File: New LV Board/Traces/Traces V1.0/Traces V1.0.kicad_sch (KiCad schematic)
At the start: 13 parts, among them J1 B15B-PH-K-S, J2 B15B-PH-K-S, J3 B15B-PH-K-S, J4 Conn_01x12, J5 VBATT +, J6 Conn_01x12, J7 Conn_01x12, J8 Vs

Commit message: minor changes to traces
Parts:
- removed D1: BZV55B15, Diode_SMD:D_SC-80_HandSoldering, symbol BZV55B15:BZV55B15
- removed TP1, TP2: 5006, TestPoint:TestPoint_Keystone_5010-5014_Multipurpose, symbol 5006:5006
- added D2: D_Zener, Diode_SMD:D_1210_3225Metric, symbol Device:D_Zener
- added TP3, TP4: TestPoint, TestPoint:TestPoint_Keystone_5005-5009_Compact, symbol Connector:TestPoint
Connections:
- net at C2.1, J5.1, J8.2: now also D2.2 (A), TP4.1
- net at C2.2, F1.1, F1.2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: now also D2.1 (K), TP3.1
- net at J1.2, J4.10 (Pin_10), J4.11 (Pin_11)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: now also J7.8 (Pin_8); no longer J7.1 (Pin_1), J7.2 (Pin_2), J7.7 (Pin_7)
- net at J1.3, J4.7 (Pin_7), J6.8 (Pin_8): now also J7.4 (Pin_4); no longer J7.8 (Pin_8)
- net at J1.7: now also J7.2 (Pin_2); no longer J7.6 (Pin_6)
- net at J3.4: now also J7.1 (Pin_1); no longer J7.12 (Pin_12)
- net at J4.6 (Pin_6), J4.8 (Pin_8), J6.7 (Pin_7): now also J7.7 (Pin_7); no longer J7.3 (Pin_3), J7.9 (Pin_9)
- net at J7.5 (Pin_5): now also J3.6; no longer J3.1
- net at J3.7: now also J7.6 (Pin_6)
- new net: J3.5, J7.3 (Pin_3)
- now unconnected: J7.10 (Pin_10)
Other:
- note added: "5v"
- note added: "From PC"
- note added: "From enable switch"
- note added: "PC Status"
- note added: "VCU - Throttle latchinG"
- note added: "VCU Charge Enable"
- note removed: "5V+"
- note removed: "PC STATUS"
- note removed: "Precharge COIL"
- note removed: "TSMS VS"
- note removed: "VCU - Throttle latching - Precharge"

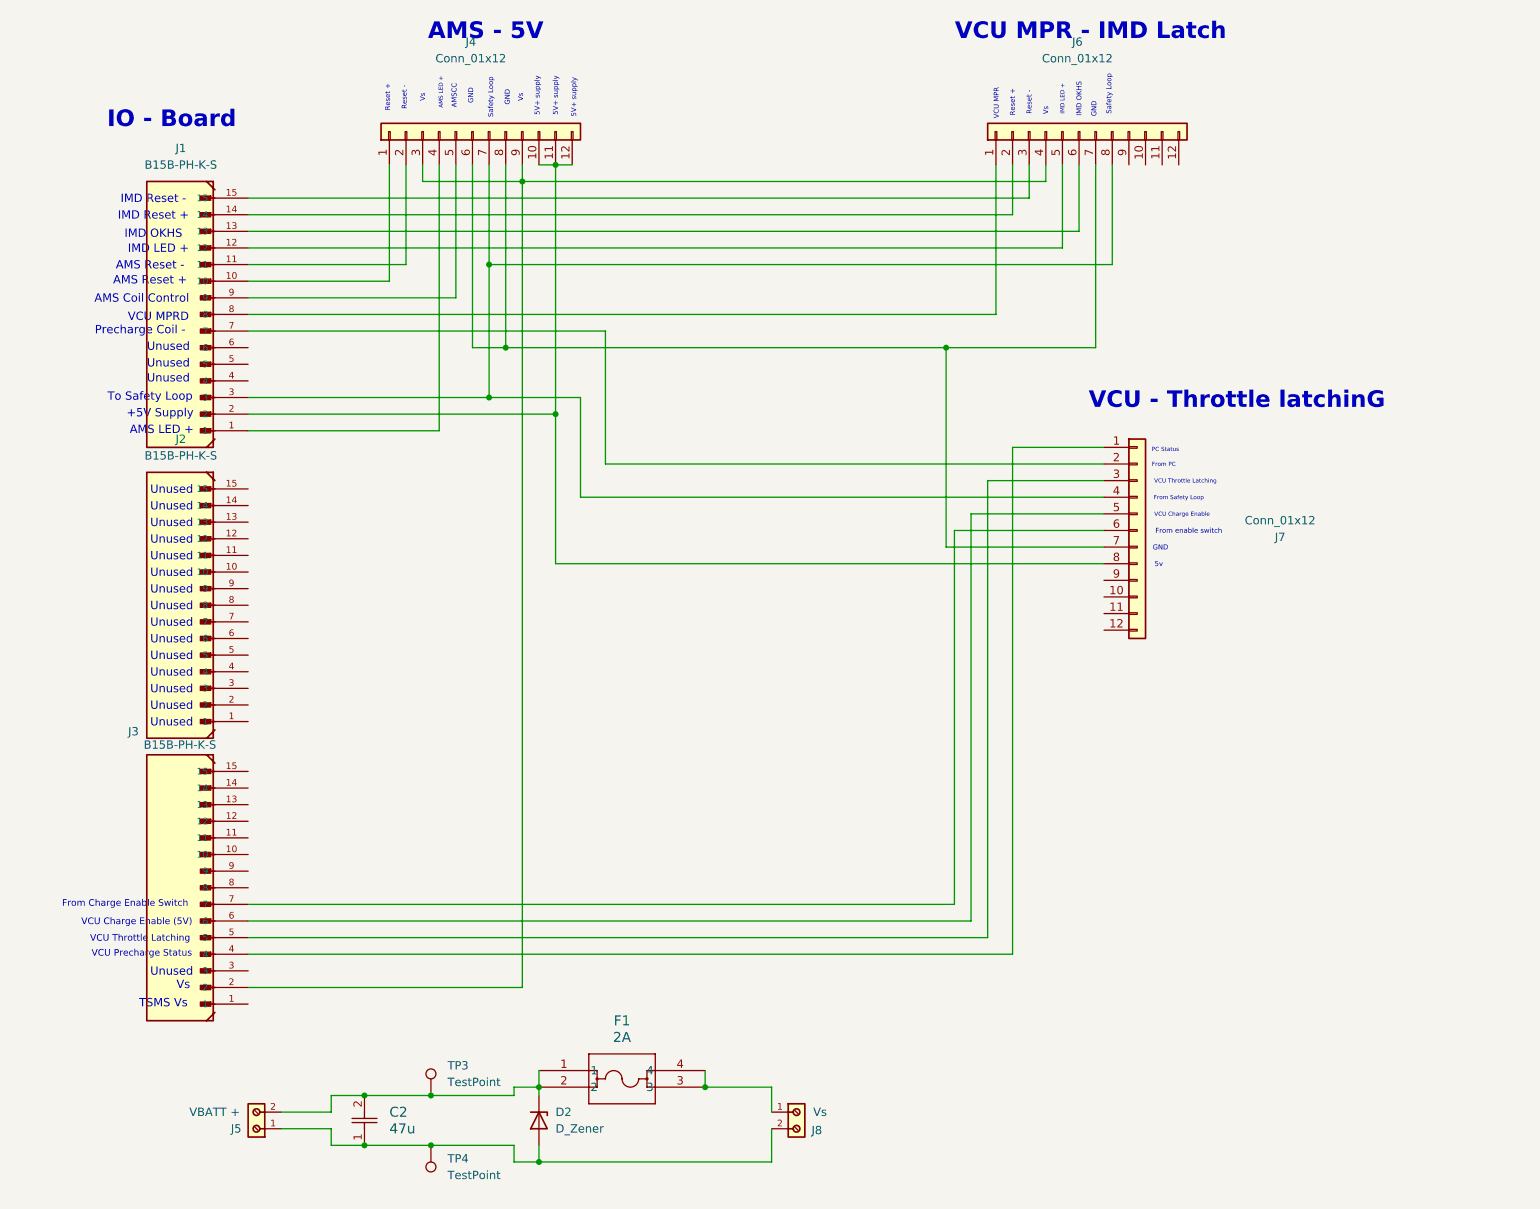
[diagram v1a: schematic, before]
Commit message: minor power changes to traces schematic
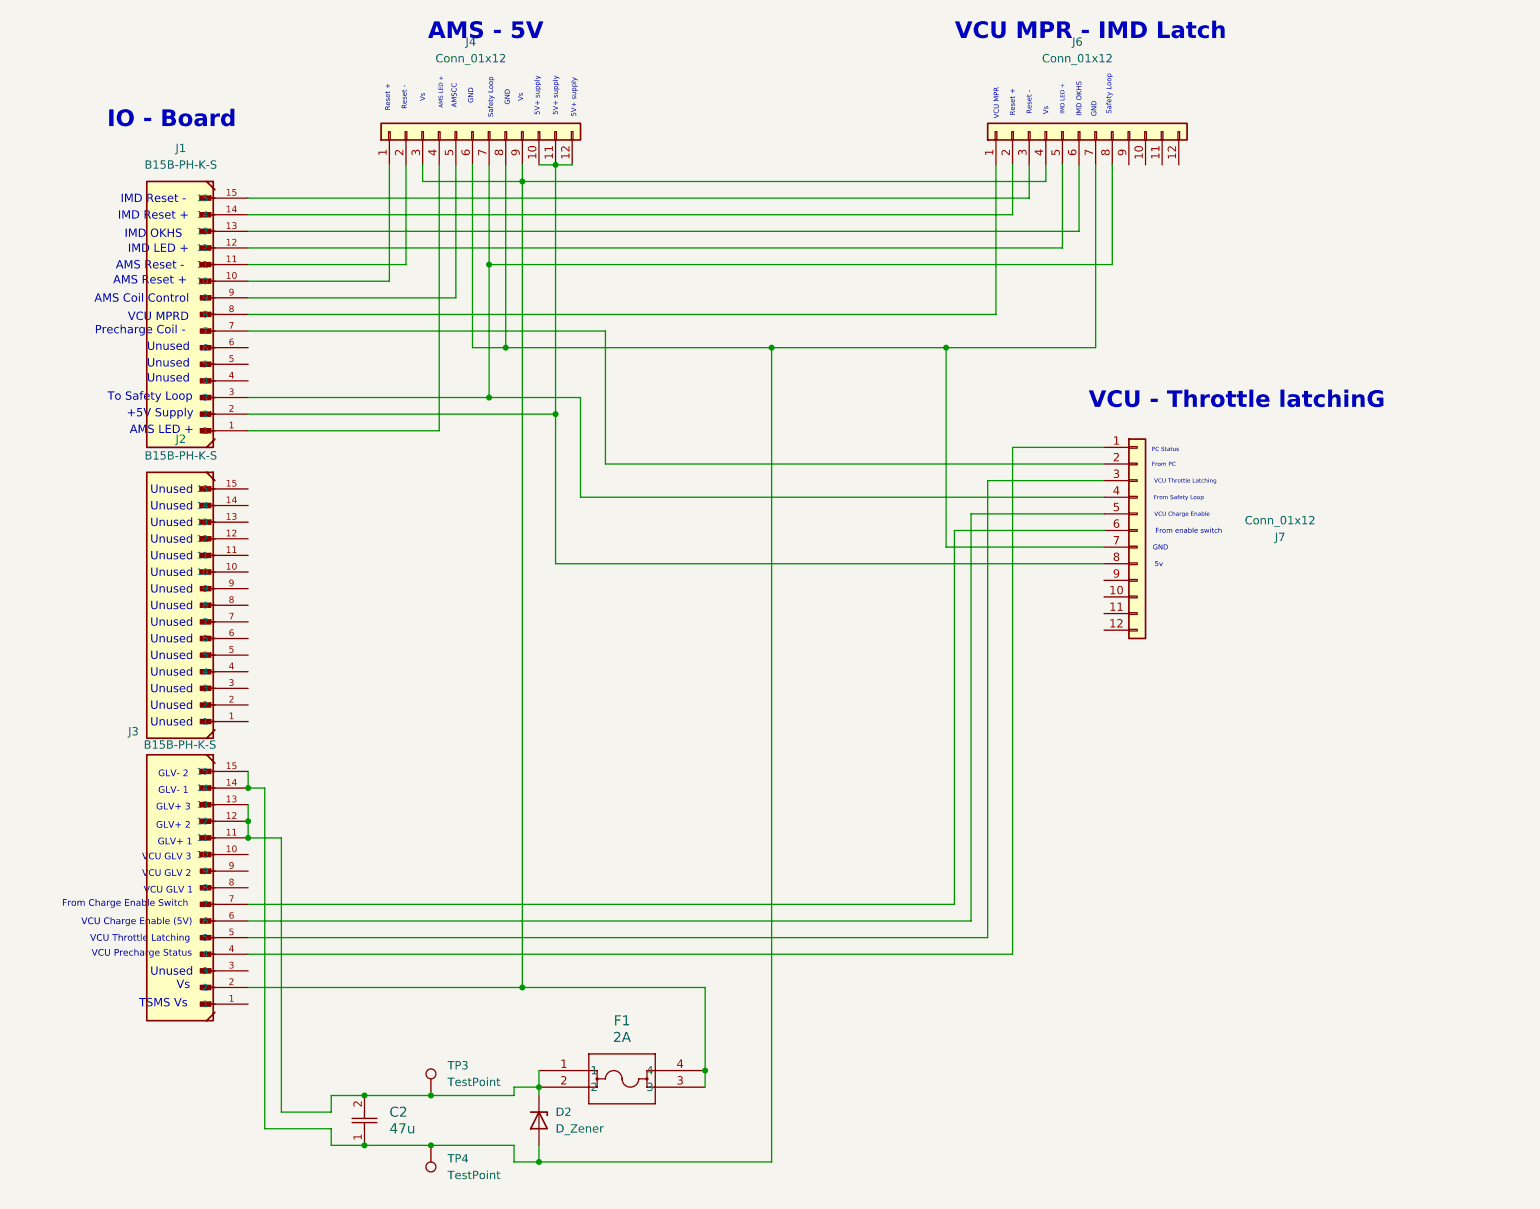
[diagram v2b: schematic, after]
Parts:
- removed J5: VBATT +, motorsports:691137710002, symbol 691137710002:691137710002
- removed J8: Vs, motorsports:691137710002, symbol 691137710002:691137710002
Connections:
- net at C2.1, D2.2 (A), TP4.1: now also J3.14, J3.15, J4.6 (Pin_6), J4.8 (Pin_8), J6.7 (Pin_7), J7.7 (Pin_7)
- net at C2.2, D2.1 (K), F1.1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: now also J3.11, J3.12, J3.13
- net at F1.3, F1.4: now also J3.2, J4.3 (Pin_3), J4.9 (Pin_9), J6.4 (Pin_4)
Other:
- note added: "GLV+ 1"
- note added: "GLV+ 2"
- note added: "GLV+ 3"
- note added: "GLV- 1"
- note added: "GLV- 2"
- note added: "VCU GLV 1"
- note added: "VCU GLV 2"
- note added: "VCU GLV 3"

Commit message: vcu throttle latching connected to traces
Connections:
- net at F1.3, F1.4, J4.3 (Pin_3)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: now also J3.4; no longer J3.2
- net at J7.1 (Pin_1): now also J3.5; no longer J3.4
- net at J7.3 (Pin_3): now also J3.6; no longer J3.5
- net at J7.5 (Pin_5): now also J3.7; no longer J3.6
- net at J7.6 (Pin_6): now also J3.8; no longer J3.7
- net at J3.1: now also J3.10, J3.9
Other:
- note added: "VCU - Throttle latching"
- note removed: "TSMS Vs"
- note removed: "VCU - Throttle latchinG"

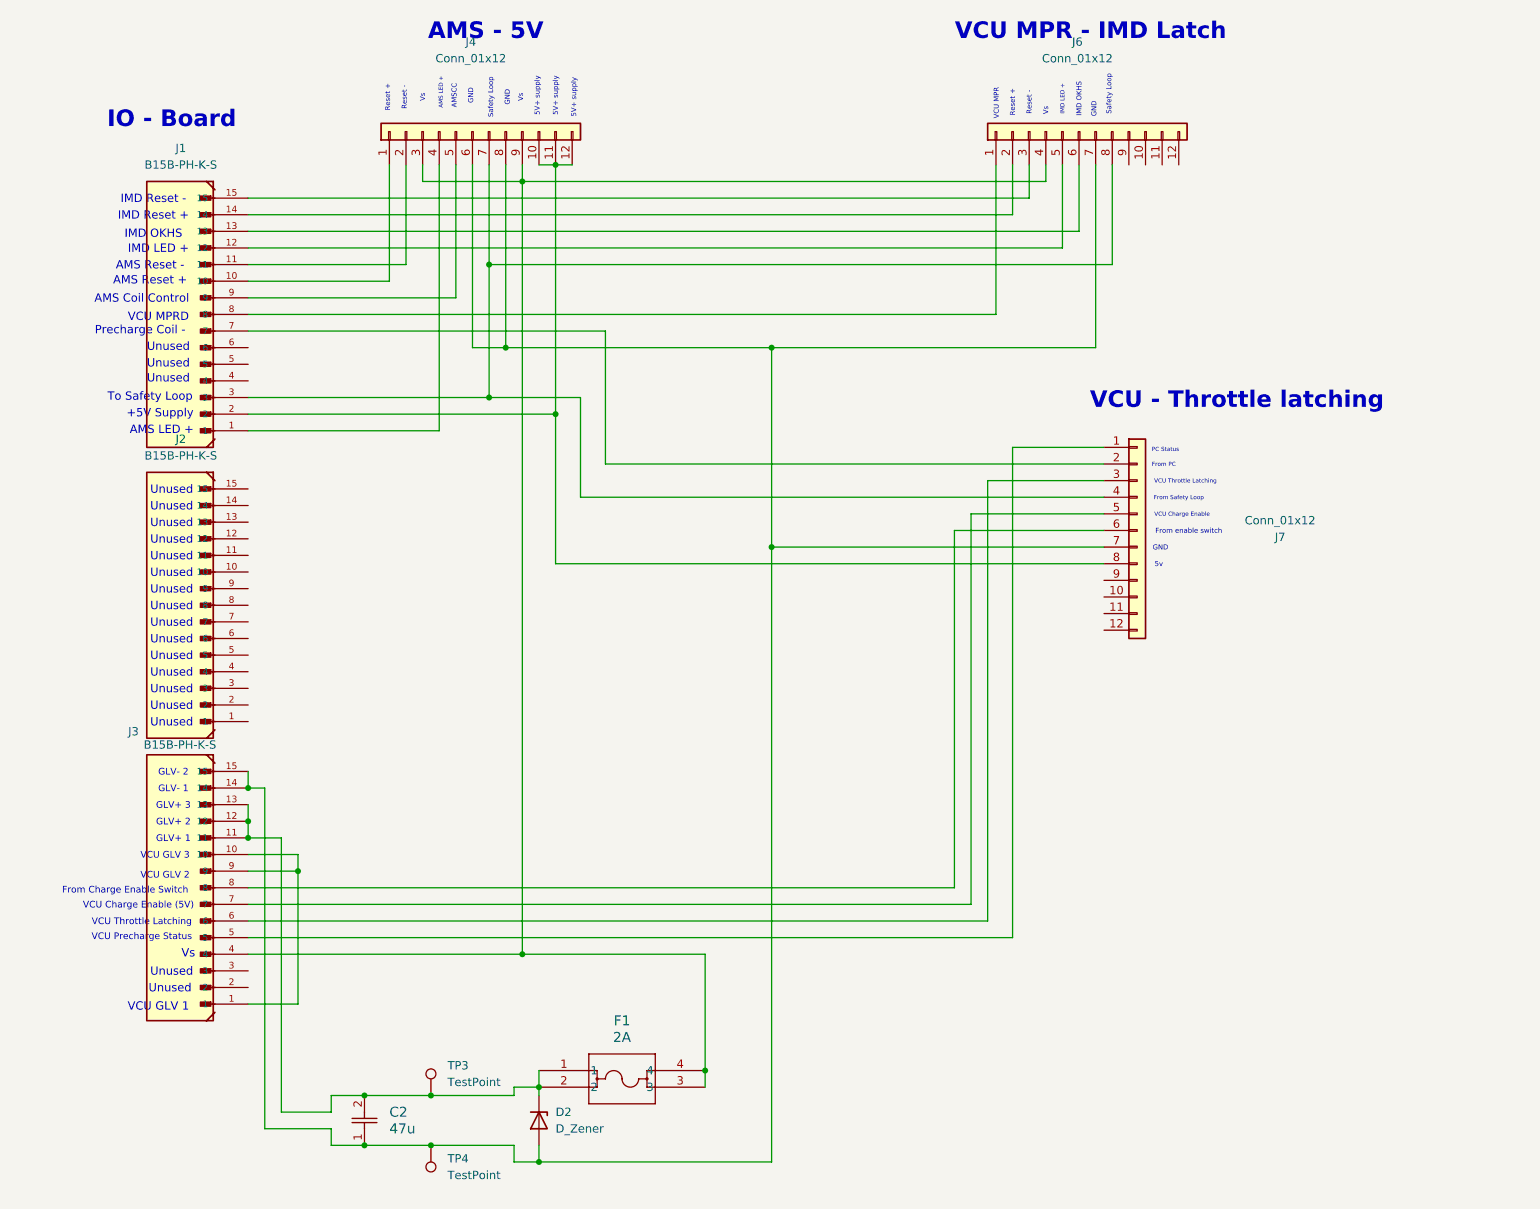
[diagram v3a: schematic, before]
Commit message: added VCU MPR - 5V to scehematic
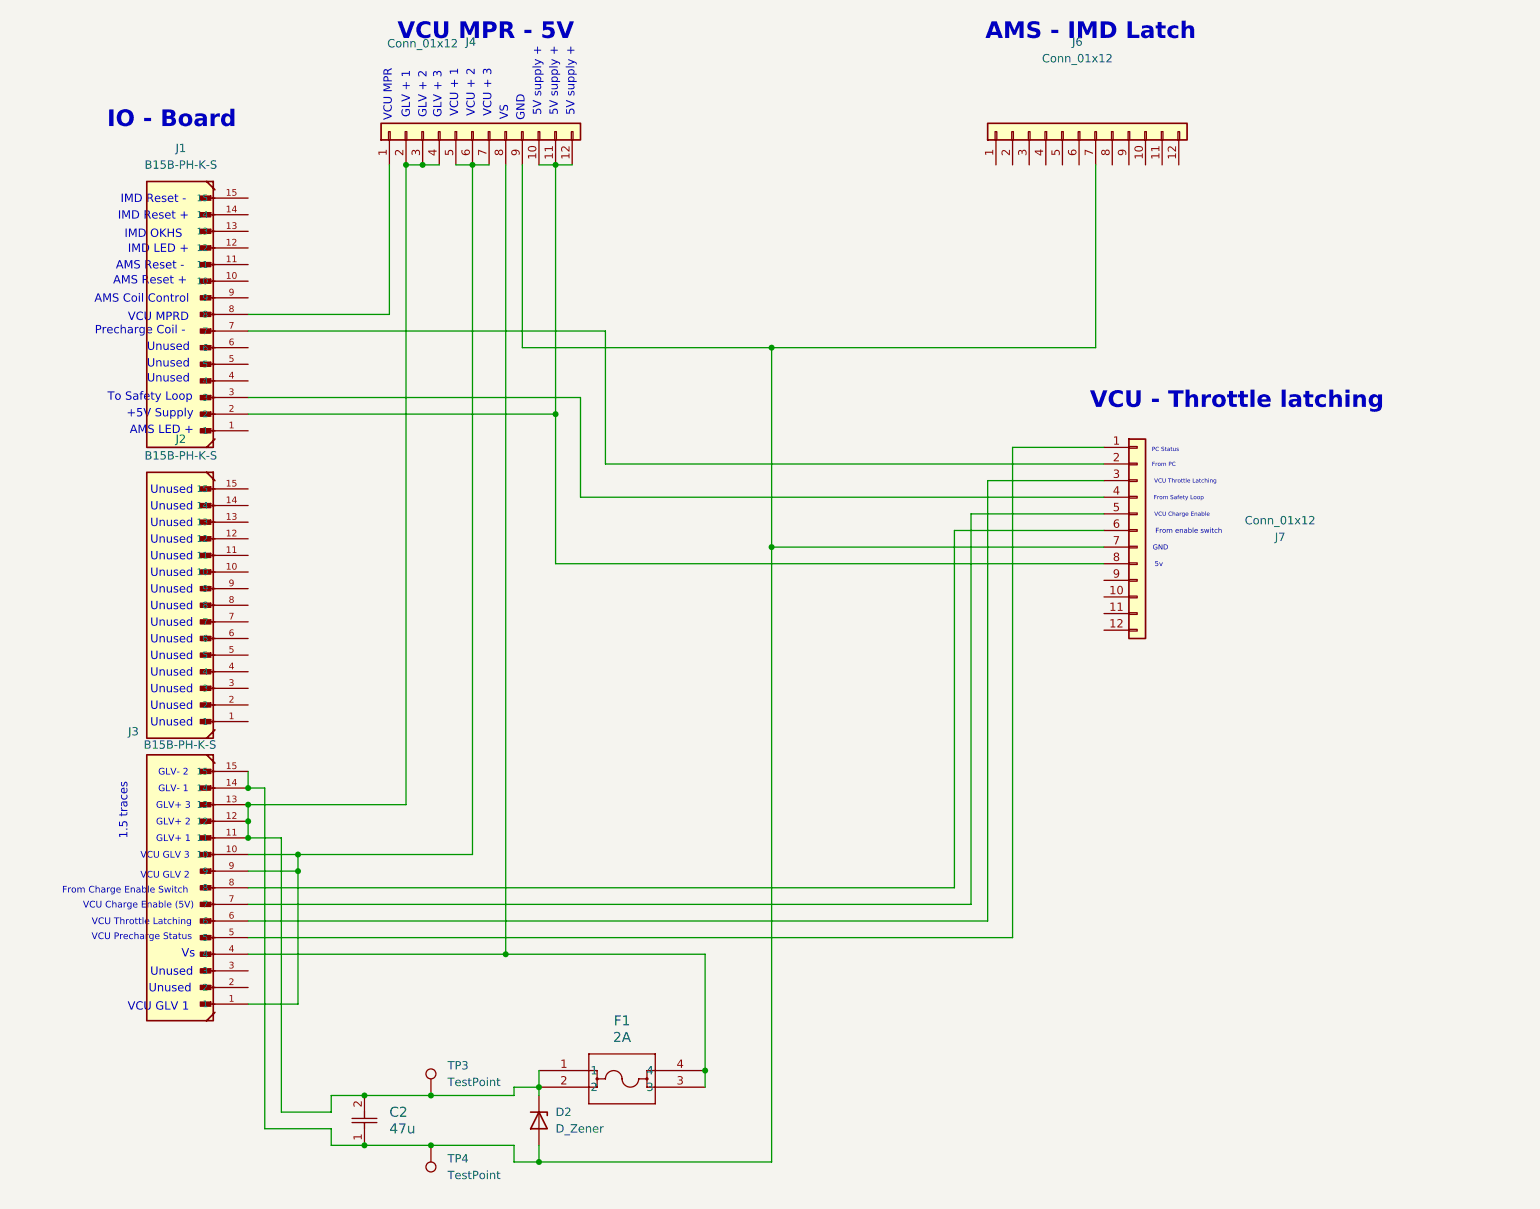
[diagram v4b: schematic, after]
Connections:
- net at J1.1: no longer J4.4 (Pin_4)
- net at J1.10: no longer J4.1 (Pin_1)
- net at J1.11: no longer J4.2 (Pin_2)
- net at J1.12: no longer J6.5 (Pin_5)
- net at J1.13: no longer J6.6 (Pin_6)
- net at J1.14: no longer J6.2 (Pin_2)
- net at J1.15: no longer J6.3 (Pin_3)
- net at J1.3, J7.4 (Pin_4): no longer J4.7 (Pin_7), J6.8 (Pin_8)
- net at J1.8: now also J4.1 (Pin_1); no longer J6.1 (Pin_1)
- net at J1.9: no longer J4.5 (Pin_5)
- net at C2.2, D2.1 (K), F1.1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: now also J4.2 (Pin_2), J4.3 (Pin_3), J4.4 (Pin_4)
- net at F1.3, F1.4, J3.4: now also J4.8 (Pin_8); no longer J4.3 (Pin_3), J4.9 (Pin_9), J6.4 (Pin_4)
- net at C2.1, D2.2 (A), J3.14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: now also J4.9 (Pin_9); no longer J4.6 (Pin_6), J4.8 (Pin_8)
- net at J3.1, J3.10, J3.9: now also J4.5 (Pin_5), J4.6 (Pin_6), J4.7 (Pin_7)
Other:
- note added: "1.5 traces"
- note added: "5V supply +"
- note added: "AMS - IMD Latch"
- note added: "GLV + 1"
- note added: "GLV + 2"
- note added: "GLV + 3"
- note added: "VCU + 1"
- note added: "VCU + 2"
- note added: "VCU + 3"
- note added: "VCU MPR - 5V"
- note added: "VS"
- note removed: "5V+ supply"
- note removed: "AMS - 5V"
- note removed: "AMSCC"
- note removed: "Reset +"
- note removed: "Reset -"
- note removed: "Safety Loop"
- note removed: "VCU MPR - IMD Latch"
